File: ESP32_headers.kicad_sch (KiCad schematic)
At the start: 2 parts, among them J1 Conn_01x15_Socket, J2 Conn_01x15_Socket

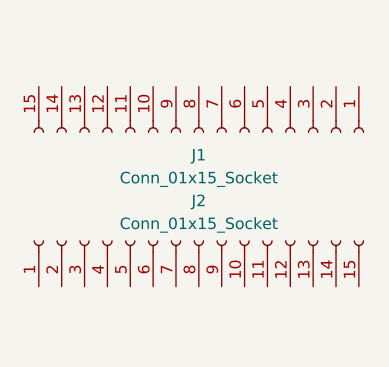
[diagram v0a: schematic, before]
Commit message: adds labels
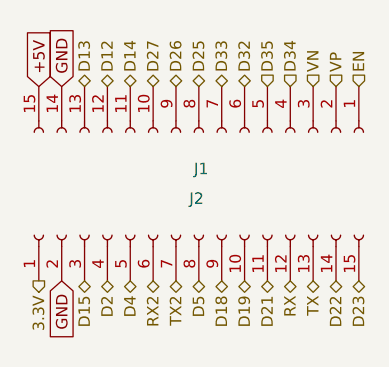
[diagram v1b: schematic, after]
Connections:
- net EN: now reaches J1.1 (Pin_1)
- net D27: now reaches J1.10 (Pin_10)
- net D14: now reaches J1.11 (Pin_11)
- net D12: now reaches J1.12 (Pin_12)
- net D13: now reaches J1.13 (Pin_13)
- net GND: now reaches J1.14 (Pin_14)
- net GND: now also J2.2 (Pin_2)
- net +5V: now reaches J1.15 (Pin_15)
- net VP: now reaches J1.2 (Pin_2)
- net VN: now reaches J1.3 (Pin_3)
- net D34: now reaches J1.4 (Pin_4)
- net D35: now reaches J1.5 (Pin_5)
- net D32: now reaches J1.6 (Pin_6)
- net D33: now reaches J1.7 (Pin_7)
- net D25: now reaches J1.8 (Pin_8)
- net D26: now reaches J1.9 (Pin_9)
- net 3.3V: now reaches J2.1 (Pin_1)
- net D19: now reaches J2.10 (Pin_10)
- net D21: now reaches J2.11 (Pin_11)
- net RX: now reaches J2.12 (Pin_12)
- net TX: now reaches J2.13 (Pin_13)
- net D22: now reaches J2.14 (Pin_14)
- net D23: now reaches J2.15 (Pin_15)
- net D15: now reaches J2.3 (Pin_3)
- net D2: now reaches J2.4 (Pin_4)
- net D4: now reaches J2.5 (Pin_5)
- net RX2: now reaches J2.6 (Pin_6)
- net TX2: now reaches J2.7 (Pin_7)
- net D5: now reaches J2.8 (Pin_8)
- net D18: now reaches J2.9 (Pin_9)
